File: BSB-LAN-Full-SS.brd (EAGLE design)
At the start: 86.5 x 49.4 mm, 122 parts, among them IC1 LAN8710A-EZC, IC2 TPS2376DDA, IC3 TX4138, IC4 SY8089AAAC, IC6 CH340X, Q1 BC847, Q2 BC857, Q3 BC847, Q4 WPM2015-3/TR, Q5 BC847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

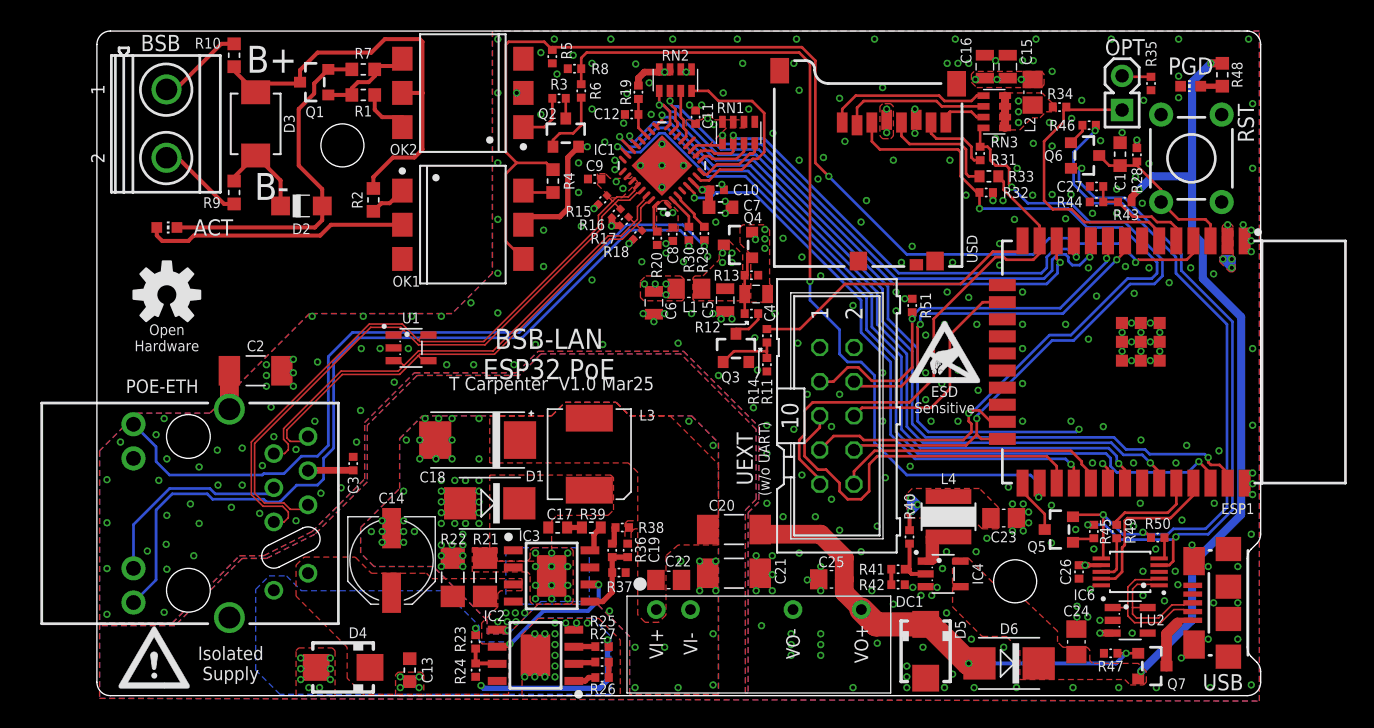
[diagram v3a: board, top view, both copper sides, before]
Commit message: Change Stackup to JLC Default 4L
Use the default stack-up using 7628 to allow the use of Economic assembly. Update trace widths of diff pairs accordingly.
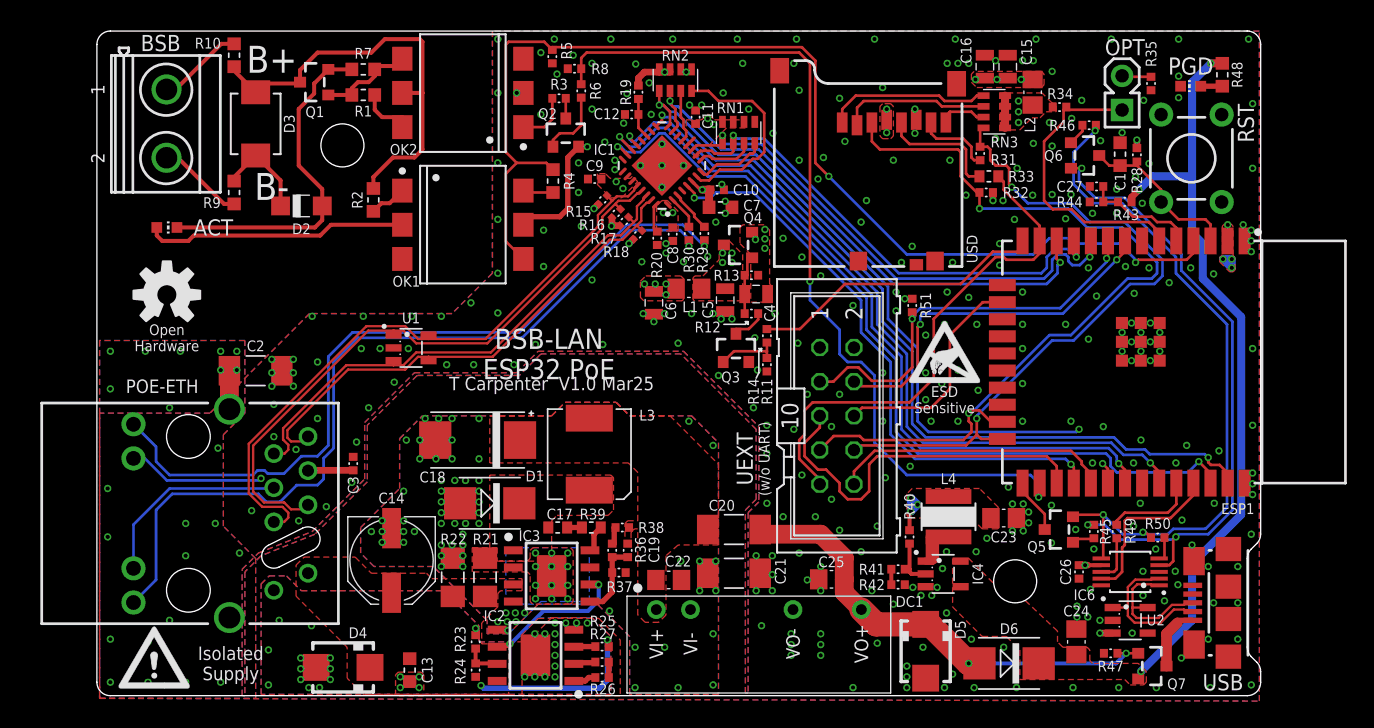
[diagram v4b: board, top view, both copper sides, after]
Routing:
- net GND: track 0.00 -> 9.96 mm, vias 340 -> 317
- net ETH-TD_P: track 47.9 -> 47.1 mm
- net ETH-TD_N: track 48.6 -> 47.8 mm
- net ETH-RD_P: track 38.6 -> 37.9 mm
- net ETH-RD_N: track 39.2 -> 38.6 mm
- net POE-V-: vias 27 -> 31
- net ETH-SHLD: vias 0 -> 23
- added copper zone on layer 1, net ETH-SHLD
- added copper zone on layer 15, net ETH-SHLD
- added copper zone on layer 16, net ETH-SHLD
- added copper zone on layer 2, net ETH-SHLD

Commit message: Fix CNMB/3 Terminal Positions
And realign PCB components to the new coordinates. This is based on measurements of the 3D model in Solidworks.

The ethernet connector has also been realigned to be central within three terminal blocks to make it easier to cut out its opening,
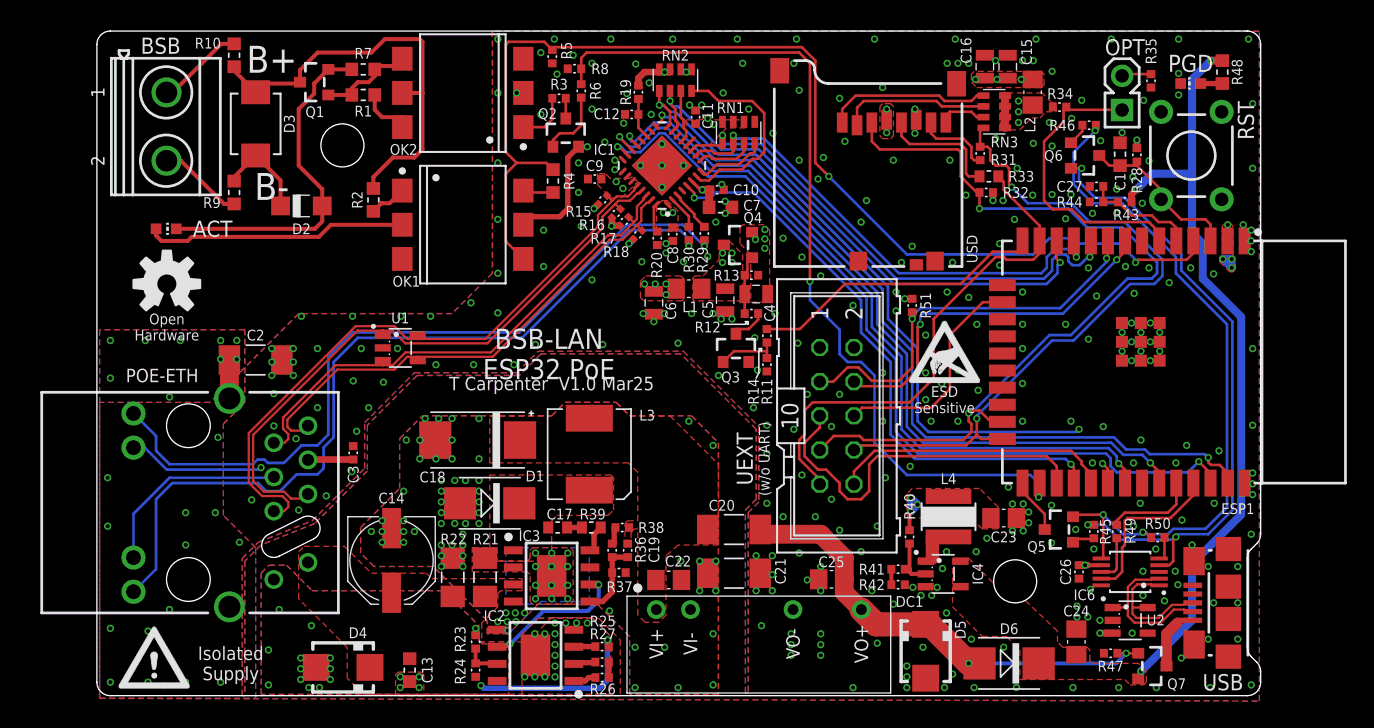
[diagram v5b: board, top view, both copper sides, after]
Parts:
- moved C3 0.80 mm to (19.1, 18.2)
- moved POE-ETH 0.80 mm to (6.80, 14.6)
- moved U$3 0.80 mm to (5.20, 30.8)
- moved U1 0.80 mm to (22.6, 26.1)
- moved C2 0.80 mm to (11.8, 25.1)
- moved BSB 0.20 mm to (5.15, 42.5)
- moved PGD 0.20 mm to (81.3, 45.7)
- moved RST 0.20 mm to (81.3, 40.3)
- moved R35 0.20 mm to (78.3, 45.9)
- moved R48 0.20 mm to (83.7, 46.5)
- moved ACT 0.11 mm to (5.15, 34.9)
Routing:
- net ETH-LED-G-K: track 62.2 -> 61.4 mm
- net ETH-VDDA: track 61.3 -> 60.5 mm
- net ETH-LED1-A: track 57.5 -> 56.7 mm

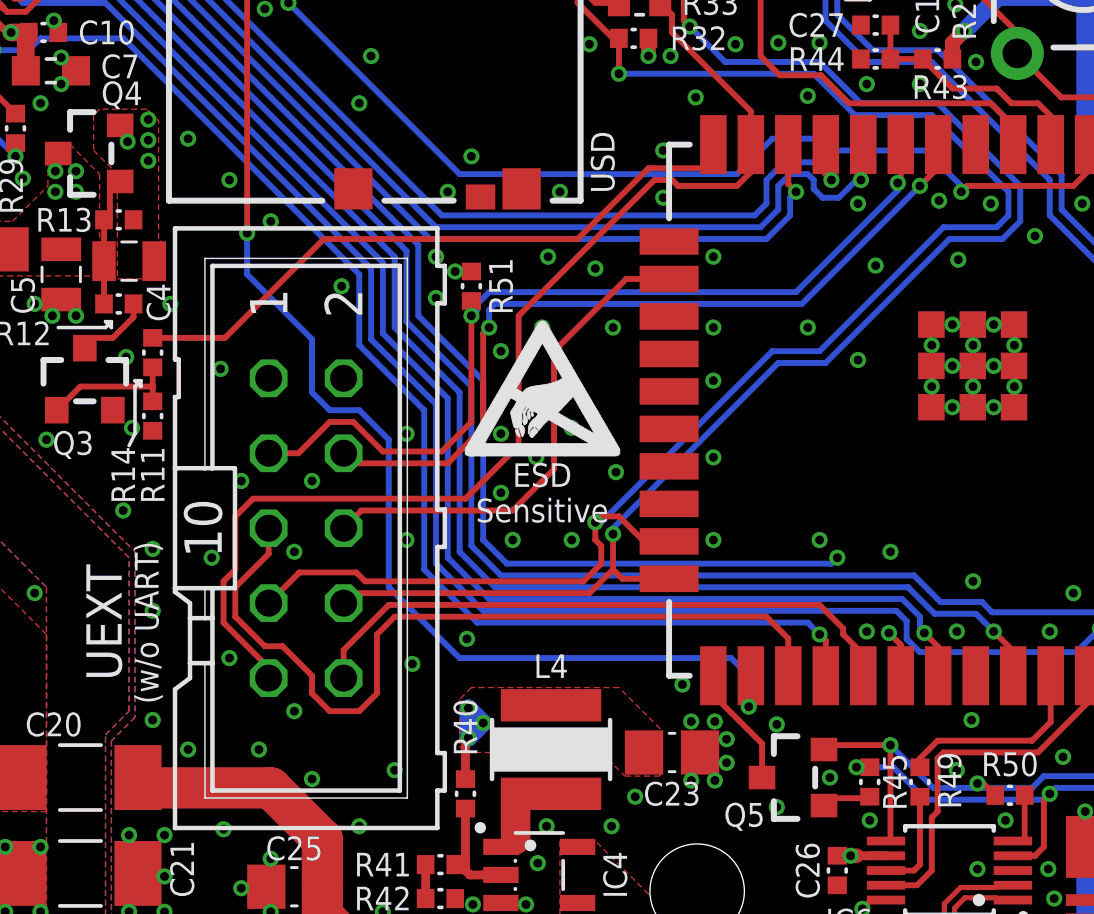
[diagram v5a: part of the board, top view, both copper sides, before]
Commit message: Add Missing Pull-Up Resistors on I2C
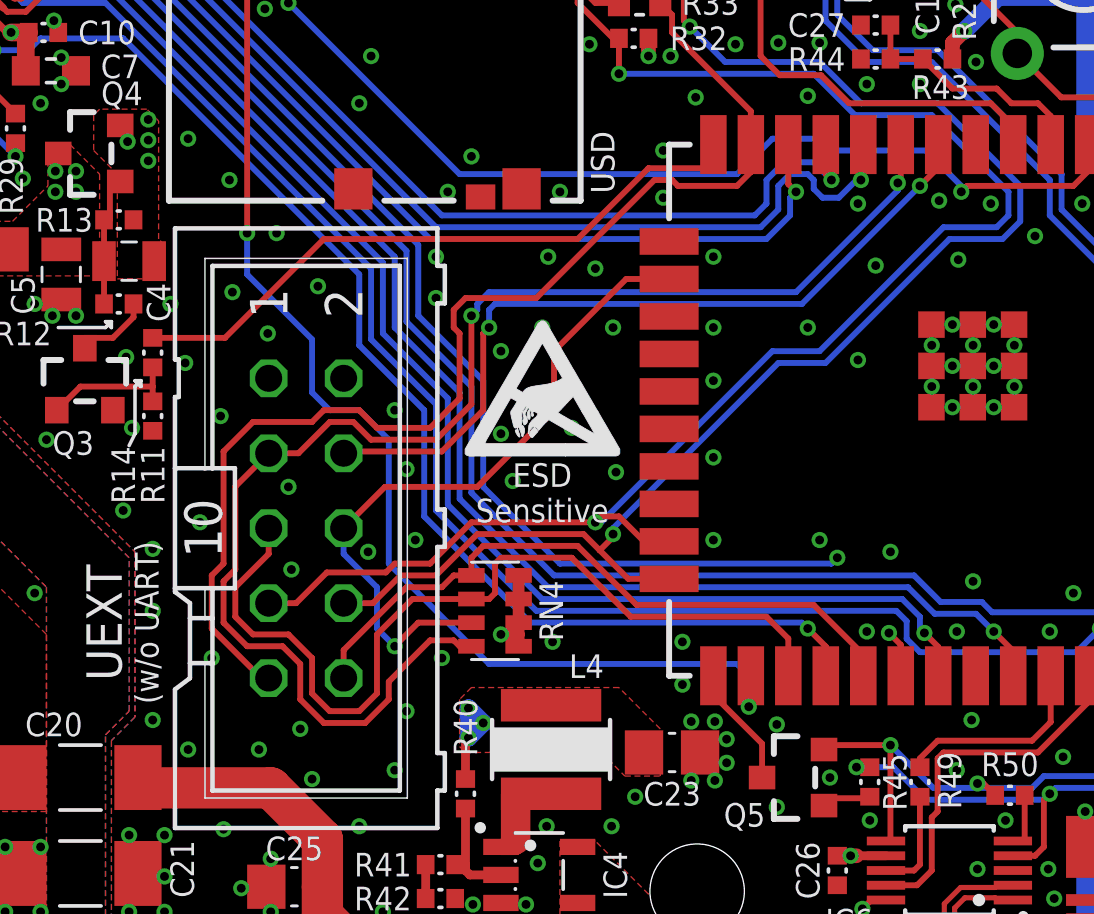
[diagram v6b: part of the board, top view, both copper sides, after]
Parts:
- removed R51: 10k, BSB-LAN:R0402
- added RN4: 2.2k, BSB-LAN:CTS742C083
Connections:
- net +3.3V: now also RN4.5, RN4.6, RN4.7, RN4.8; no longer R51.1
- net ESP-SCL: now also RN4.2
- net ESP-SDA: now also RN4.3
- net ESP-SSEL: now also RN4.1
- net UEXT-TX: now also RN4.4; no longer R51.2
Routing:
- net UEXT-TX: track 30.2 -> 47.5 mm
- net ESP-SDA: track 16.9 -> 23.3 mm, vias 0 -> 1
- net ESP-SCL: track 27.9 -> 30.5 mm
- net +3.3V: track 46.4 -> 48.9 mm
- net ESP-SD-CLK: track 38.3 -> 40.3 mm
- net ESP-SSEL: track 20.7 -> 22.6 mm
- net ESP-SD-CMD: track 63.7 -> 62.3 mm
- net EMAC-CLKOUT: track 43.7 -> 42.5 mm
- net EMAC-TXEN: track 57.3 -> 56.3 mm
- net EMAC-TXD1: track 62.6 -> 61.5 mm
- net EMAC-TXD0: track 56.3 -> 55.3 mm
- net EMAC-MDIO: track 54.0 -> 53.0 mm
- net EMAC-MDC: track 59.6 -> 58.5 mm
- net UEXT-RX: track 27.4 -> 26.8 mm
- net GND: vias 317 -> 320

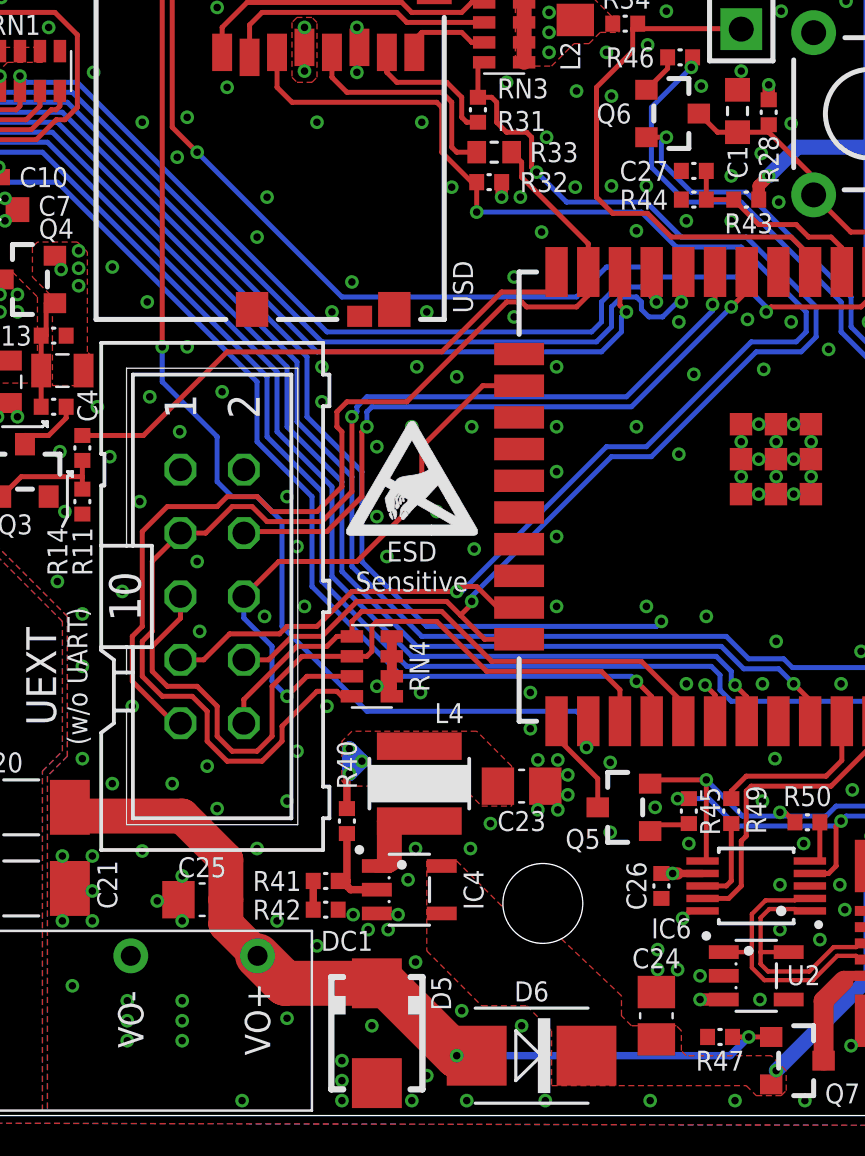
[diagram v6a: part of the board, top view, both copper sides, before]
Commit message: Correct Pinout of DC-DC Converter
Not sure quite how I messed up the pin assignments that badly!
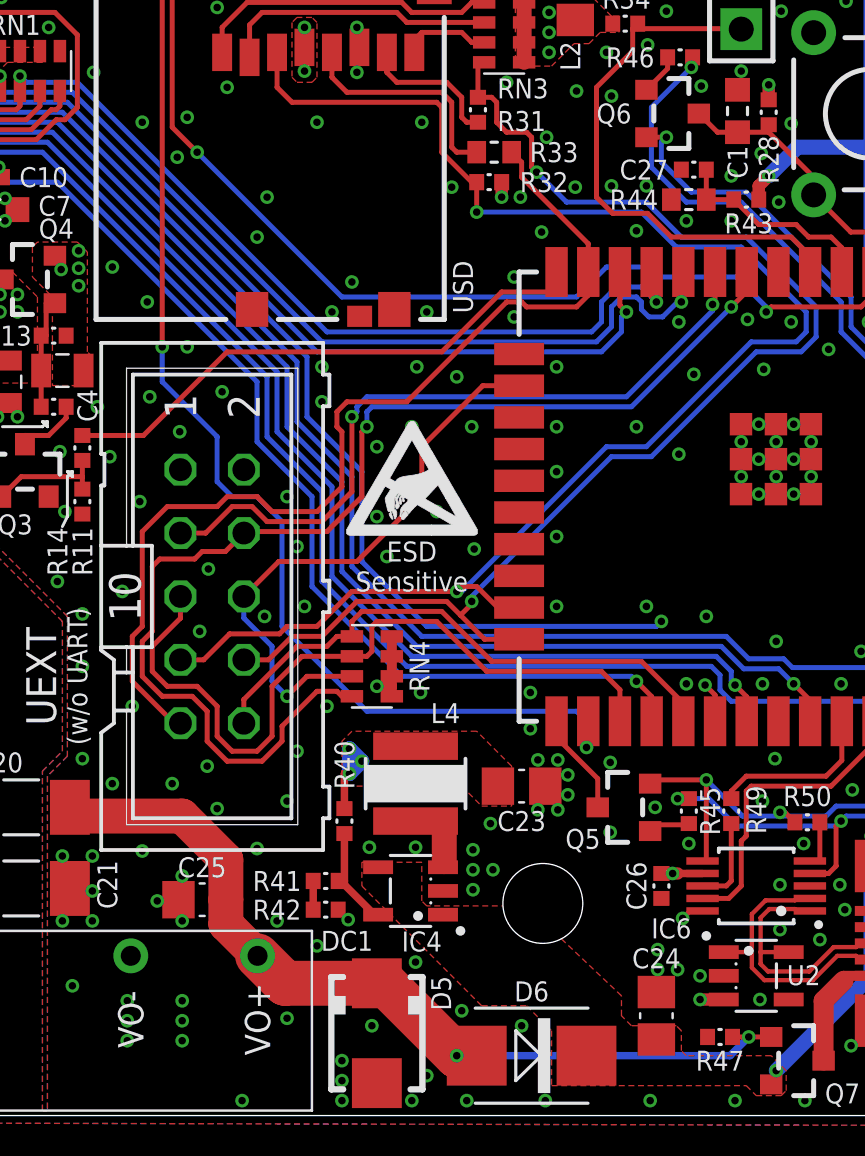
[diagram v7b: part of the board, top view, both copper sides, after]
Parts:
- R43: value 12.1k 1% -> 180k 1%
- R44: value 28.7k 1% -> 330k; device BSB-LAN:R0402 -> BSB-LAN:R0603L
- RST: value Tact-RA -> Tact 19mm
- moved R44 0.20 mm to (74.1, 36.9)
- moved L4 0.15 mm to (63.1, 13.5)
- moved R40 0.10 mm to (60.3, 12.0)
- moved IC4 0.07 mm to (63.0, 9.20), turned to 90 degrees
- moved C27 0.05 mm to (74.3, 38.1)
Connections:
- removed net POE-DC-POK-NC: IC3.7
- net +5.0V: now also IC4.1; no longer IC4.5
- net 3V3-FB: now also IC4.5; no longer IC4.2
- net 3V3-LX: now also IC4.3; no longer IC4.1
- net GND: now also IC4.2; no longer IC4.3
- net UEXT-RX: now also RN4.4
- net UEXT-TX: no longer RN4.4
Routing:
- net UEXT-RX: track 26.8 -> 47.7 mm
- net UEXT-TX: track 47.5 -> 29.0 mm
